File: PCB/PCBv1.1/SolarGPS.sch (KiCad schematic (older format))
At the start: 54 parts, among them J1 Conn_01x10_Female, J2 Solar1+, J3 GND, J4 Conn_02x05_Odd_Even, J5 Solar2+, J6 GND, J7 Screw_Terminal_01x01, U2 MAX-M10Q, U4 STM32WB5MMGH6TR, U5 BQ25505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

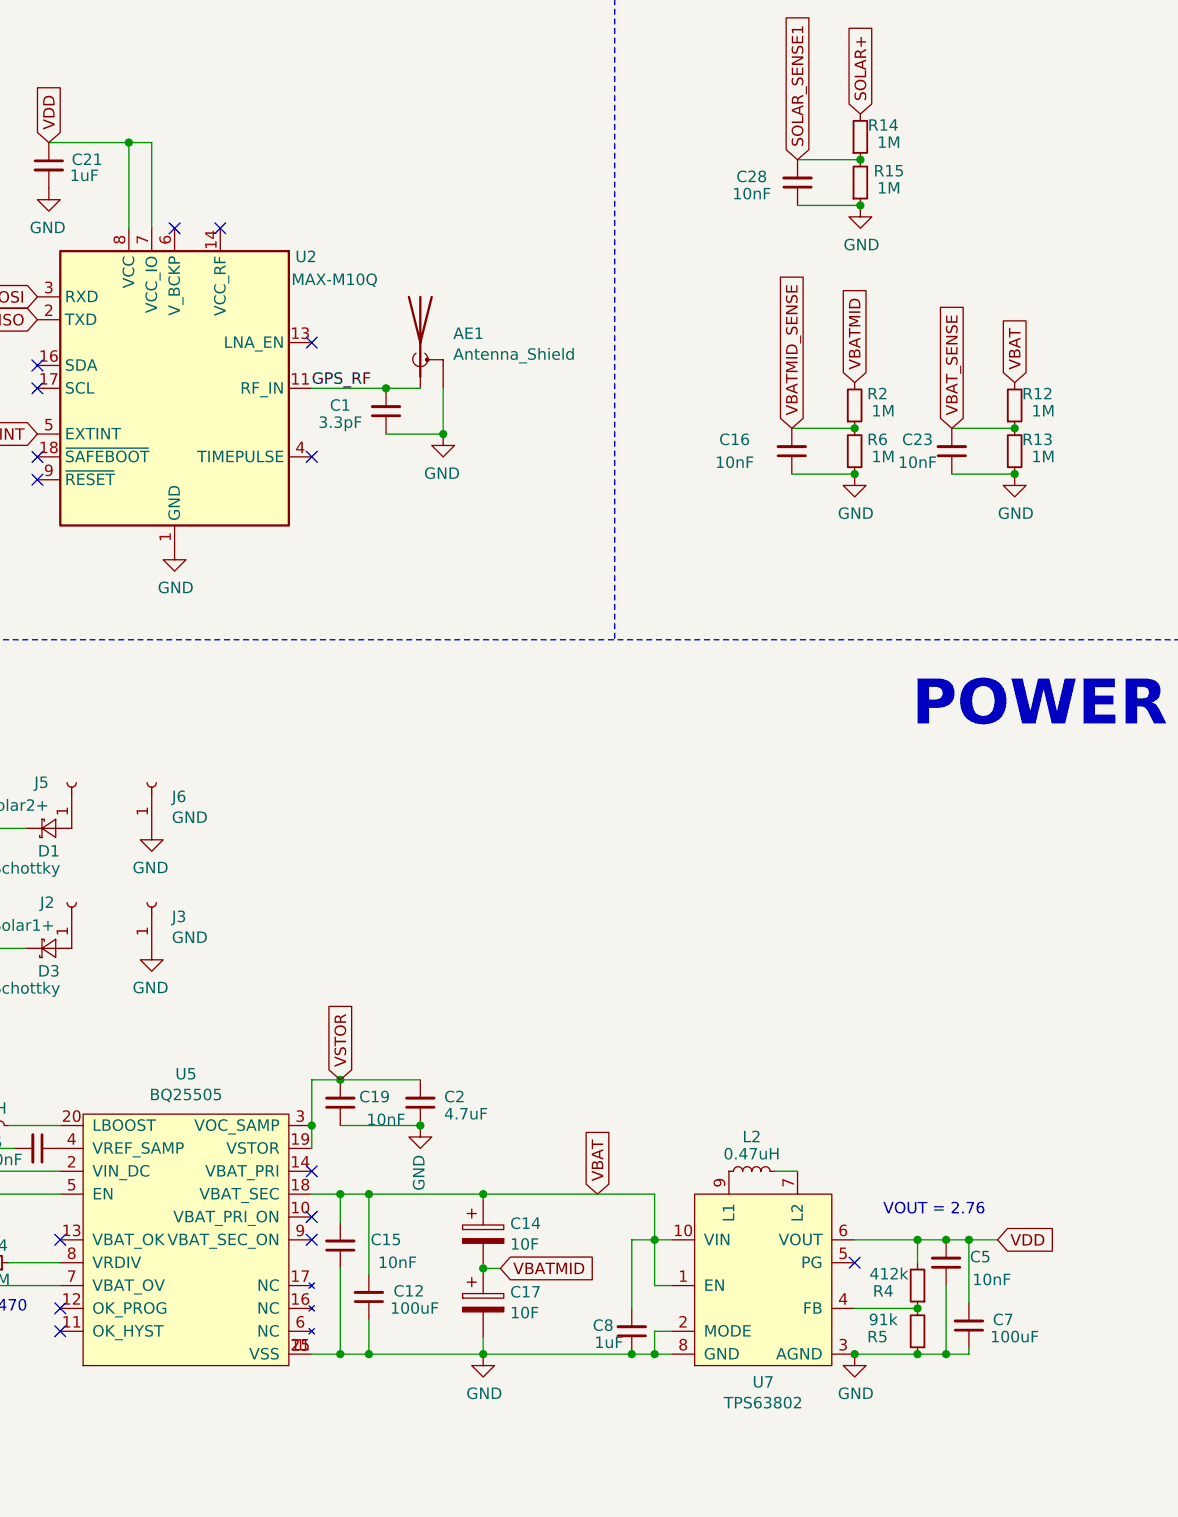
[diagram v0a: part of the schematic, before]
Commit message: Change VCC to 2.87 Remove LCD connector
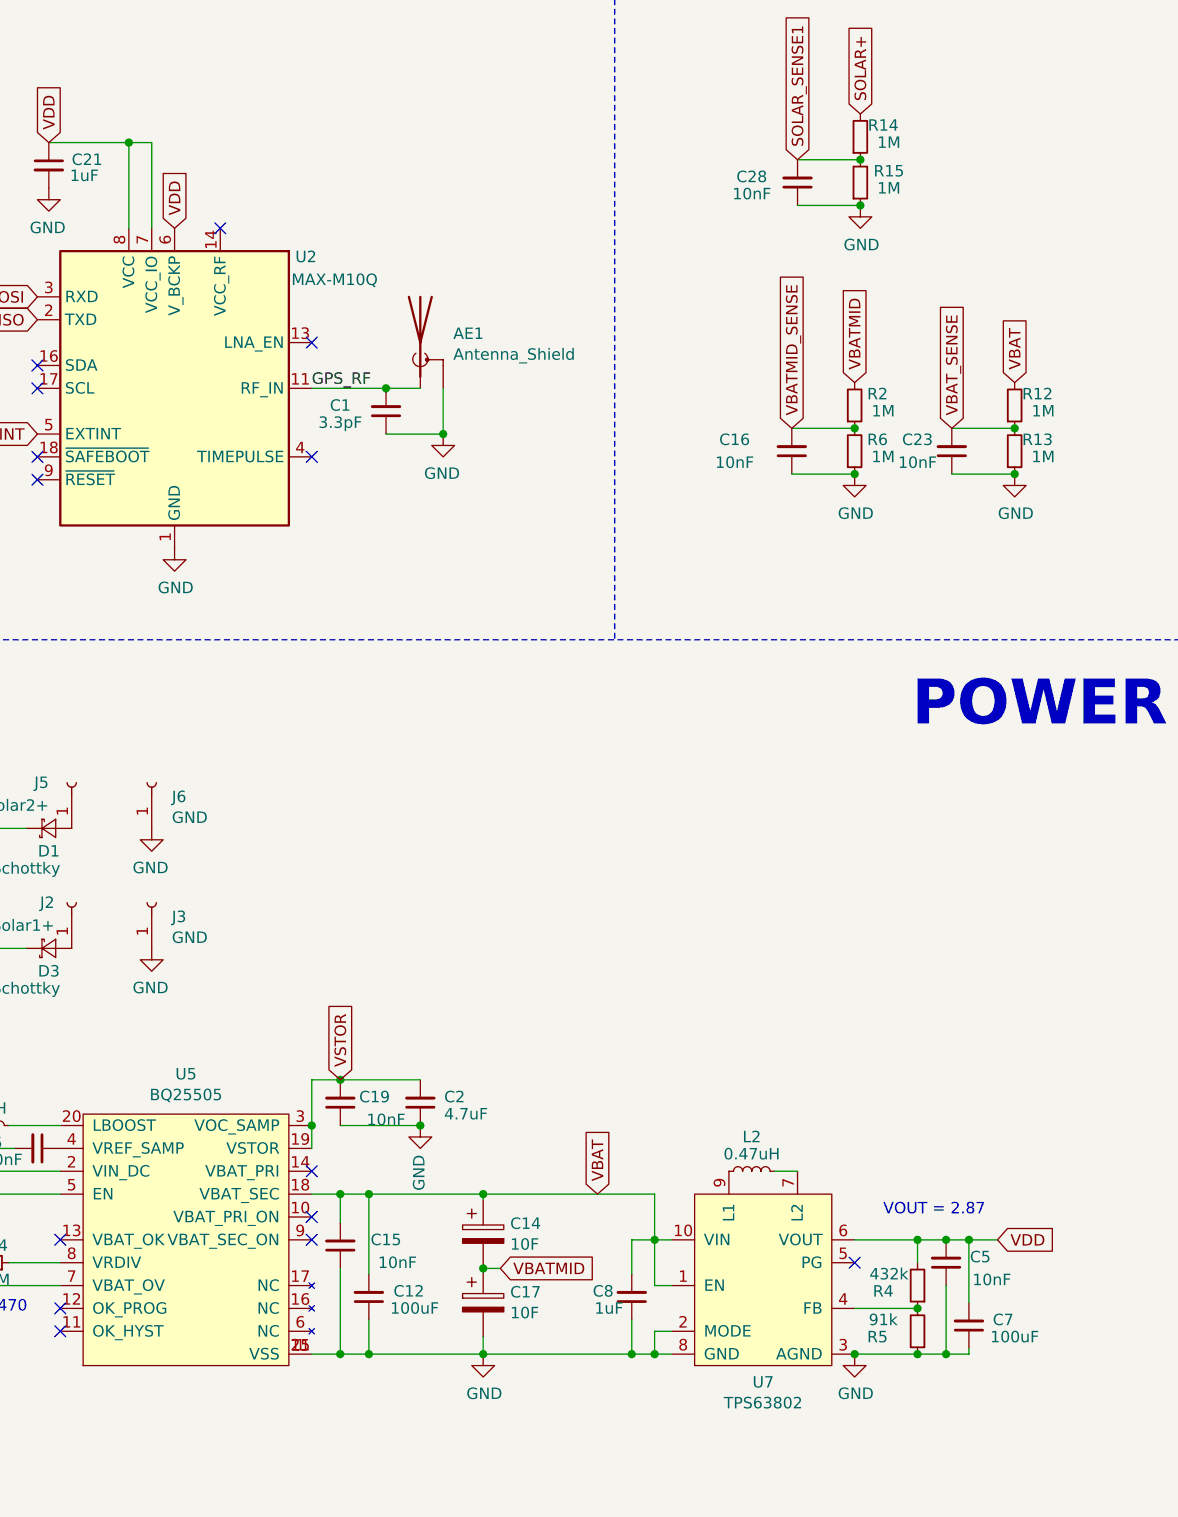
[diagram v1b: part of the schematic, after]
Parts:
- D4: footprint Diode_SMD:D_SOD-523 -> Diode_SMD:D_SOD-323_HandSoldering
- J1: footprint Margo_Lib:AYF531035 -> Veridian Designed:0.5pFlexToBoard
- R4: value 412k -> 432k
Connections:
- net VDD: now also U2.6 (V_BCKP)
- no-connect marks 25 -> 24
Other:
- note added: "VOUT = 2.87"
- note removed: "VOUT = 2.76"
- moved on the sheet: C8
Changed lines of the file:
@@
 F 0 "J1" H 7500 6200 50  0000 L CNN
 F 1 "Conn_01x10_Female" H 7125 6100 50  0000 L CNN
-F 2 "Margo_Lib:AYF531035" H 7800 5575 50  0001 C CNN
+F 2 "Veridian Designed:0.5pFlexToBoard" H 7800 5575 50  0001 C CNN
 F 3 "~" H 7800 5575 50  0001 C CNN
 	1    7800 5575
@@
 P 5525 6900
 F 0 "R4" H 5675 6925 50  0000 C CNN
-F 1 "412k" H 5650 6850 50  0000 C CNN
+F 1 "432k" H 5650 6850 50  0000 C CNN
 F 2 "Resistor_SMD:R_0603_1608Metric" H 5525 6900 50  0001 C CNN
 F 3 "~" H 5525 6900 50  0001 C CNN
@@
 L Device:C_Small C8
 U 1 1 61BA52AB
-P 4275 7100
-F 0 "C8" H 4400 7075 50  0000 C CNN
-F 1 "1uF" H 4375 7150 50  0000 C CNN
-F 2 "Capacitor_SMD:C_0603_1608Metric" H 4275 7100 50  0001 C CNN
-F 3 "~" H 4275 7100 50  0001 C CNN
-	1    4275 7100
+P 4275 6950
+F 0 "C8" H 4400 6925 50  0000 C CNN
+F 1 "1uF" H 4375 7000 50  0000 C CNN
+F 2 "Capacitor_SMD:C_0603_1608Metric" H 4275 6950 50  0001 C CNN
+F 3 "~" H 4275 6950 50  0001 C CNN
+	1    4275 6950
 	-1   0    0    1
 $EndComp
@@
 F 0 "D4" H 1100 6200 50  0000 L CNN
 F 1 "5.1V" H 1050 6125 50  0000 L CNN
-F 2 "Diode_SMD:D_SOD-523" V 1100 6050 50  0001 C CNN
+F 2 "Diode_SMD:D_SOD-323_HandSoldering" V 1100 6050 50  0001 C CNN
 F 3 "~" V 1100 6050 50  0001 C CNN
 F 4 "BZT52C5V1T-TP" H 1100 6050 50  0001 C CNN "Part"
@@
 $EndComp
 Text Notes 5375 6600 0    50   ~ 0
-VOUT = 2.76
+VOUT = 2.87
 $Comp
 L Device:C_Small C2
@@
 	0    -1   -1   0
 $EndComp
-NoConn ~ 2275 2275
 $Comp
 L Device:C_Small C21
@@
 	3625 6500 4375 6500
 Wire Wire Line
-	4275 7000 4275 6700
-Wire Wire Line
 	4275 6700 4375 6700
+Wire Wire Line
+	4275 6850 4275 6700
+Wire Wire Line
+	4275 7050 4275 7200
+Text GLabel 2275 2275 1    50   Input ~ 0
+VDD
 $EndSCHEMATC

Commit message: Cost savings!
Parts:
- removed D4: 5.1V, Diode_SMD:D_SOD-323_HandSoldering, symbol Device:D_Zener_Small
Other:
- note added: "Also See AEM10300"
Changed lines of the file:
@@
 	1    0    0    1
-$EndComp
-$Comp
-L Device:D_Zener_Small D4
-U 1 1 619FB2B4
-P 1100 6050
-F 0 "D4" H 1100 6200 50  0000 L CNN
-F 1 "5.1V" H 1050 6125 50  0000 L CNN
-F 2 "Diode_SMD:D_SOD-323_HandSoldering" V 1100 6050 50  0001 C CNN
-F 3 "~" V 1100 6050 50  0001 C CNN
-F 4 "BZT52C5V1T-TP" H 1100 6050 50  0001 C CNN "Part"
-	1    1100 6050
-	-1   0    0    -1
 $EndComp
 Text GLabel 3000 6000 1    50   Input ~ 0
@@
 	0    -1   -1   0
 $EndComp
-Wire Wire Line
-	1200 6050 1350 6050
-Connection ~ 1350 6050
-Wire Wire Line
-	1350 6050 1350 6200
-Wire Wire Line
-	1000 6050 1000 6200
-Connection ~ 1000 6200
 $Comp
 L power:GND #PWR0104
@@
 Wire Wire Line
 	1625 5425 1350 5425
-Wire Wire Line
-	1350 5425 1350 6050
 Wire Wire Line
 	1625 4900 1350 4900
@@
 Text GLabel 2275 2275 1    50   Input ~ 0
 VDD
+Text Notes 1700 7500 0    50   ~ 0
+Also See AEM10300
+Wire Wire Line
+	1350 5425 1350 6200
 $EndSCHEMATC

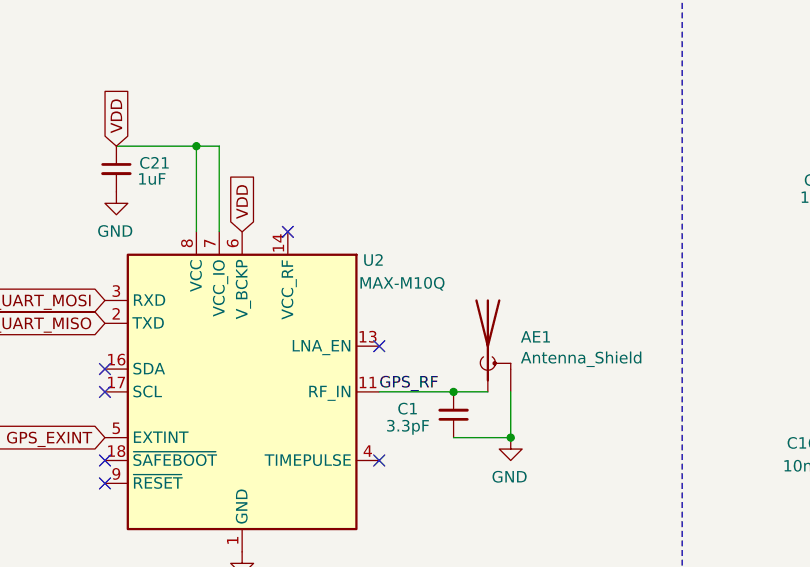
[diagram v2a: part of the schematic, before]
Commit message: tweak PCB1.1 add some notes
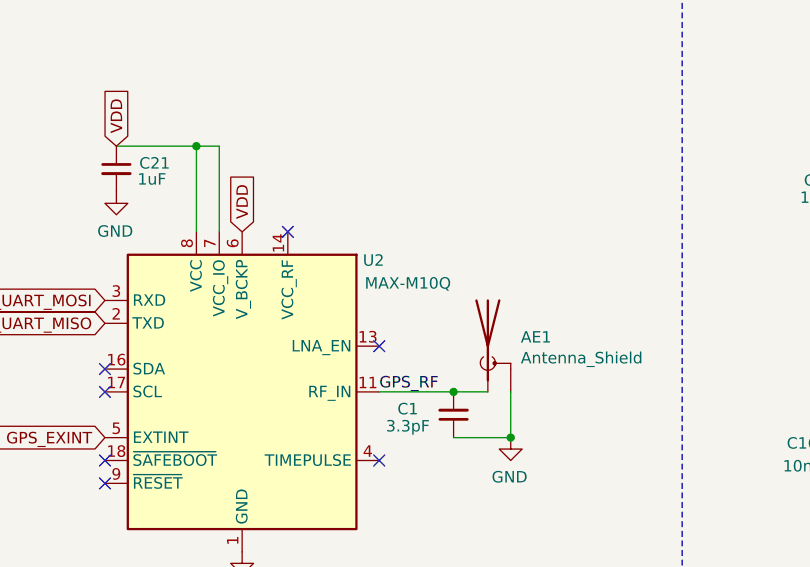
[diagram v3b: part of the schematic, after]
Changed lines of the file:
@@
 P 2275 2975
 F 0 "U2" H 2850 3550 50  0000 C CNN
-F 1 "MAX-M10Q" H 2975 3450 50  0000 C CNN
+F 1 "MAX-M10Q" H 3000 3450 50  0000 C CNN
 F 2 "RF_GPS:ublox_MAX" H 2675 2325 50  0001 C CNN
 F 3 "https://www.u-blox.com/sites/default/files/MAX-M8-FW3_DataSheet_%28UBX-15031506%29.pdf" H 2275 2975 50  0001 C CNN

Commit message: Play with USB idea. Update to KiCad 5
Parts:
- removed AE1: Antenna_Shield, RF_Antenna:Pulse_W3011, symbol Device:Antenna_Shield
- removed C1, C10, C11, C13: 3.3pF, Capacitor_SMD:C_0402_1005Metric, symbol Device:C_Small
- removed C12, C7: 100uF, Capacitor_SMD:C_1206_3216Metric, symbol Device:C_Small
- removed C14, C17: 10F, Veridian-Library-KiCad:SCCT20E106SRB, symbol Device:CP
- removed C15, C16, C18, C19, C23, C28, C5, C6: 10nF, Capacitor_SMD:C_0603_1608Metric, symbol Device:C_Small
- removed C2, C3: 4.7uF, Capacitor_SMD:C_0805_2012Metric, symbol Device:C_Small
- removed C20, C21, C25, C26, C8, C9: 1uF, Capacitor_SMD:C_0603_1608Metric, symbol Device:C_Small
- removed D1, D3: Schottky, Diode_SMD:D_SOD-323_HandSoldering, symbol Device:D_Schottky_Small
- removed D2: LED, Diode_SMD:D_0805_2012Metric, symbol Device:LED
- removed J1: Conn_01x10_Female, Veridian Designed:0.5pFlexToBoard, symbol Connector:Conn_01x10_Female
- removed J2: Solar1+, Connector_PinHeader_2.54mm:PinHeader_1x01_P2.54mm_Vertical, symbol Connector:Conn_01x01_Female
- removed J3, J6: GND, Connector_PinHeader_2.54mm:PinHeader_1x01_P2.54mm_Vertical, symbol Connector:Conn_01x01_Female
- removed J4: Conn_02x05_Odd_Even, Connector_PinHeader_2.00mm:PinHeader_2x05_P2.00mm_Vertical_SMD, symbol Connector_Generic:Conn_02x05_Odd_Even
- removed J5: Solar2+, Connector_PinHeader_2.54mm:PinHeader_1x01_P2.54mm_Vertical, symbol Connector:Conn_01x01_Female
- removed J7: Screw_Terminal_01x01, Veridian-Library-KiCad:Right Angle Screw Terminal M3M4, symbol Connector:Screw_Terminal_01x01
- removed L2: 0.47uH, Inductor_SMD:L_0806_2016Metric, symbol Device:L_Small
- removed L3: 22uH, Inductor_SMD:L_1210_3225Metric, symbol Device:L_Small
- removed R12, R13, R14, R15, R2, R6: 1M, Resistor_SMD:R_0603_1608Metric, symbol Device:R_Small
- removed R3: 390, Resistor_SMD:R_0603_1608Metric, symbol Device:R_Small
- removed R4: 432k, Resistor_SMD:R_0603_1608Metric, symbol Device:R_Small
- removed R5: 91k, Resistor_SMD:R_0603_1608Metric, symbol Device:R_Small
- removed ROV3: 4.30M, Resistor_SMD:R_0603_1608Metric, symbol Device:R_Small
- removed ROV4: 8.66M, Resistor_SMD:R_0603_1608Metric, symbol Device:R_Small
- removed U2: MAX-M10Q, RF_GPS:ublox_MAX, symbol RF_GPS:MAX-M8Q
- removed U4: STM32WB5MMGH6TR, Veridian-Library-KiCad:XCVR_STM32WB5MMGH6TR, symbol SolarGPS-rescue:STM32WB5MMGH6TR-VeridianDesigns
- removed U5: BQ25505, Package_DFN_QFN:QFN-20-1EP_3.5x3.5mm_P0.5mm_EP2x2mm_ThermalVias, symbol MargoGeneral:BQ25505
- removed U6: LIS3DH, Package_LGA:LGA-16_3x3mm_P0.5mm_LayoutBorder3x5y, symbol Sensor_Motion:LIS3DH
- removed U7: TPS63802, Margo_Lib:VREG_TPS63802DLAR, symbol SolarGPS-rescue:TPS63802-VeridianDesigns
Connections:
- no-connect marks 24 -> 0
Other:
- note removed: "ACCEL"
- note removed: "ANALOG"
- note removed: "Also See AEM10300"
- note removed: "DISP"
- note removed: "GPS"
- note removed: "MCU+BLE"
- note removed: "MECHANICAL"
- note removed: "POWER"
- note removed: "VBATOV = 5.470"
- note removed: "VOUT = 2.87"
